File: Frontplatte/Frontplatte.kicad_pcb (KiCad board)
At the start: 2 copper layers, 49 parts, among them J1 Conn_01x04_Male, J2 Conn_01x04_Male, J3 Conn_01x04_Male, J4 Conn_01x04_Male, J5 Conn_01x04_Male, SW1 SW_DIP_x04, U1 MCP23017_SP

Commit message: Updated
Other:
- board outline added: 215.1 x 58.4 mm
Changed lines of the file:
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@@
     )
   )
-  (gr_line (start 34.925 102.235) (end 34.925 43.815) (layer "F.SilkS") (width 0.15))
-  (gr_line (start 54.61 50.165) (end 54.61 74.295) (layer "F.SilkS") (width 0.15))
-  (gr_line (start 125.73 74.295) (end 125.73 50.165) (layer "F.SilkS") (width 0.15))
-  (gr_line (start 64.77 102.235) (end 34.925 102.235) (layer "F.SilkS") (width 0.15))
-  (gr_line (start 250.063 102.235) (end 50.165 102.235) (layer "F.SilkS") (width 0.15))
-  (gr_line (start 170.18 83.8835) (end 170.18 102.235) (layer "F.SilkS") (width 0.15))
-  (gr_line (start 125.73 50.165) (end 54.61 50.165) (layer "F.SilkS") (width 0.15))
-  (gr_line (start 34.925 43.815) (end 250.063 43.815) (layer "F.SilkS") (width 0.15))
-  (gr_line (start 34.925 83.82) (end 62.23 83.82) (layer "F.SilkS") (width 0.15))
-  (gr_line (start 62.23 83.82) (end 62.23 102.235) (layer "F.SilkS") (width 0.15))
-  (gr_line (start 250.063 83.82) (end 170.18 83.8835) (layer "F.SilkS") (width 0.15))
-  (gr_line (start 54.61 74.295) (end 125.73 74.295) (layer "F.SilkS") (width 0.15))
-  (gr_line (start 250.063 43.815) (end 250.063 102.235) (layer "F.SilkS") (width 0.15))
+  (gr_line (start 34.925 83.82) (end 34.925 43.815) (layer "Edge.Cuts") (width 0.15))
+  (gr_line (start 54.61 50.165) (end 54.61 74.295) (layer "Edge.Cuts") (width 0.15))
+  (gr_line (start 125.73 74.295) (end 125.73 50.165) (layer "Edge.Cuts") (width 0.15))
+  (gr_line (start 170.18 102.235) (end 62.23 102.235) (layer "Edge.Cuts") (width 0.15))
+  (gr_line (start 170.18 83.8835) (end 170.18 102.235) (layer "Edge.Cuts") (width 0.15))
+  (gr_line (start 125.73 50.165) (end 54.61 50.165) (layer "Edge.Cuts") (width 0.15))
+  (gr_line (start 34.925 43.815) (end 250.063 43.815) (layer "Edge.Cuts") (width 0.15))
+  (gr_line (start 34.925 83.82) (end 62.23 83.82) (layer "Edge.Cuts") (width 0.15))
+  (gr_line (start 62.23 83.82) (end 62.23 102.235) (layer "Edge.Cuts") (width 0.15))
+  (gr_line (start 250.063 83.82) (end 170.18 83.8835) (layer "Edge.Cuts") (width 0.15))
+  (gr_line (start 54.61 74.295) (end 125.73 74.295) (layer "Edge.Cuts") (width 0.15))
+  (gr_line (start 250.063 43.815) (end 250.063 83.82) (layer "Edge.Cuts") (width 0.15))
   (gr_text "VCC" (at 161.29 56.007) (layer "B.SilkS")
     (effects (font (size 1 1) (thickness 0.15)) (justify mirror))

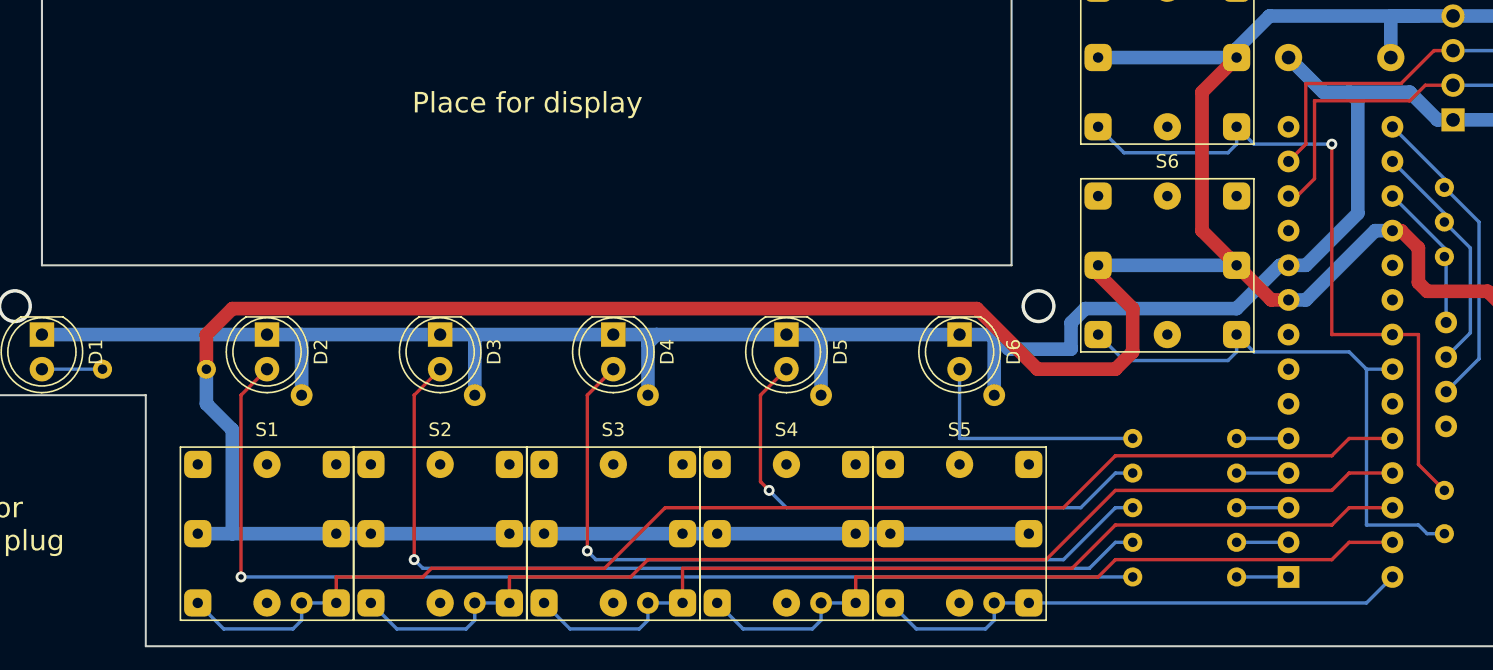
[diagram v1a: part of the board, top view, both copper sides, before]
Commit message: Inserted 3D models into Front Plate
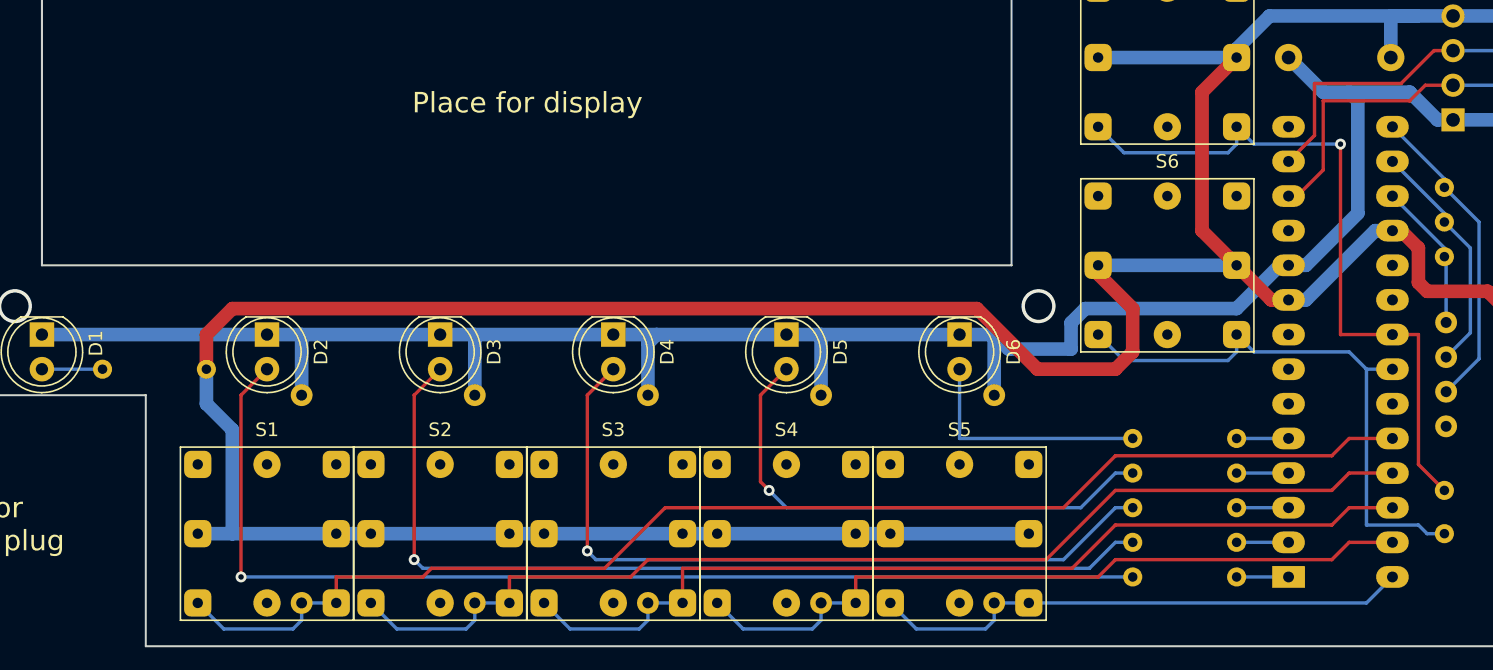
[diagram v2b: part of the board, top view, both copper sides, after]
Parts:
- U1: footprint Package_DIP:DIP-28_W7.62mm -> Package_DIP:DIP-28_W7.62mm_LongPads
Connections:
- S1 pad 1a: (no net) -> unconnected-(S1-Pad1a)
- S1 pad 1b: (no net) -> unconnected-(S1-Pad1b)
- S10 pad 1a: (no net) -> unconnected-(S10-Pad1a)
- S10 pad 1b: (no net) -> unconnected-(S10-Pad1b)
- S2 pad 1a: (no net) -> unconnected-(S2-Pad1a)
- S2 pad 1b: (no net) -> unconnected-(S2-Pad1b)
- S3 pad 1a: (no net) -> unconnected-(S3-Pad1a)
- S3 pad 1b: (no net) -> unconnected-(S3-Pad1b)
- S4 pad 1a: (no net) -> unconnected-(S4-Pad1a)
- S4 pad 1b: (no net) -> unconnected-(S4-Pad1b)
- S5 pad 1a: (no net) -> unconnected-(S5-Pad1a)
- S5 pad 1b: (no net) -> unconnected-(S5-Pad1b)
- S6 pad 1a: (no net) -> unconnected-(S6-Pad1a)
- S6 pad 1b: (no net) -> unconnected-(S6-Pad1b)
- S7 pad 1a: (no net) -> unconnected-(S7-Pad1a)
- S7 pad 1b: (no net) -> unconnected-(S7-Pad1b)
- S8 pad 1a: (no net) -> unconnected-(S8-Pad1a)
- S8 pad 1b: (no net) -> unconnected-(S8-Pad1b)
- S9 pad 1a: (no net) -> unconnected-(S9-Pad1a)
- S9 pad 1b: (no net) -> unconnected-(S9-Pad1b)
- SW1 pad 4: (no net) -> unconnected-(SW1-Pad4)
- SW1 pad 5: (no net) -> unconnected-(SW1-Pad5)
- U1 pad 11: (no net) -> unconnected-(U1-Pad11)
- U1 pad 14: (no net) -> unconnected-(U1-Pad14)
- U1 pad 19: (no net) -> unconnected-(U1-Pad19)
- U1 pad 20: (no net) -> unconnected-(U1-Pad20)
- U1 pad 23: (no net) -> unconnected-(U1-Pad23)
- U1 pad 6: (no net) -> unconnected-(U1-Pad6)
- U1 pad 7: (no net) -> unconnected-(U1-Pad7)
- U1 pad 8: (no net) -> unconnected-(U1-Pad8)
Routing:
- net Net-(R13-Pad1): track 53.2 -> 52.5 mm
